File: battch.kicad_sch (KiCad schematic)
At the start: 12 parts, among them IC1 SI3483DDV-T1-BE3, IC2 BQ25302RTER

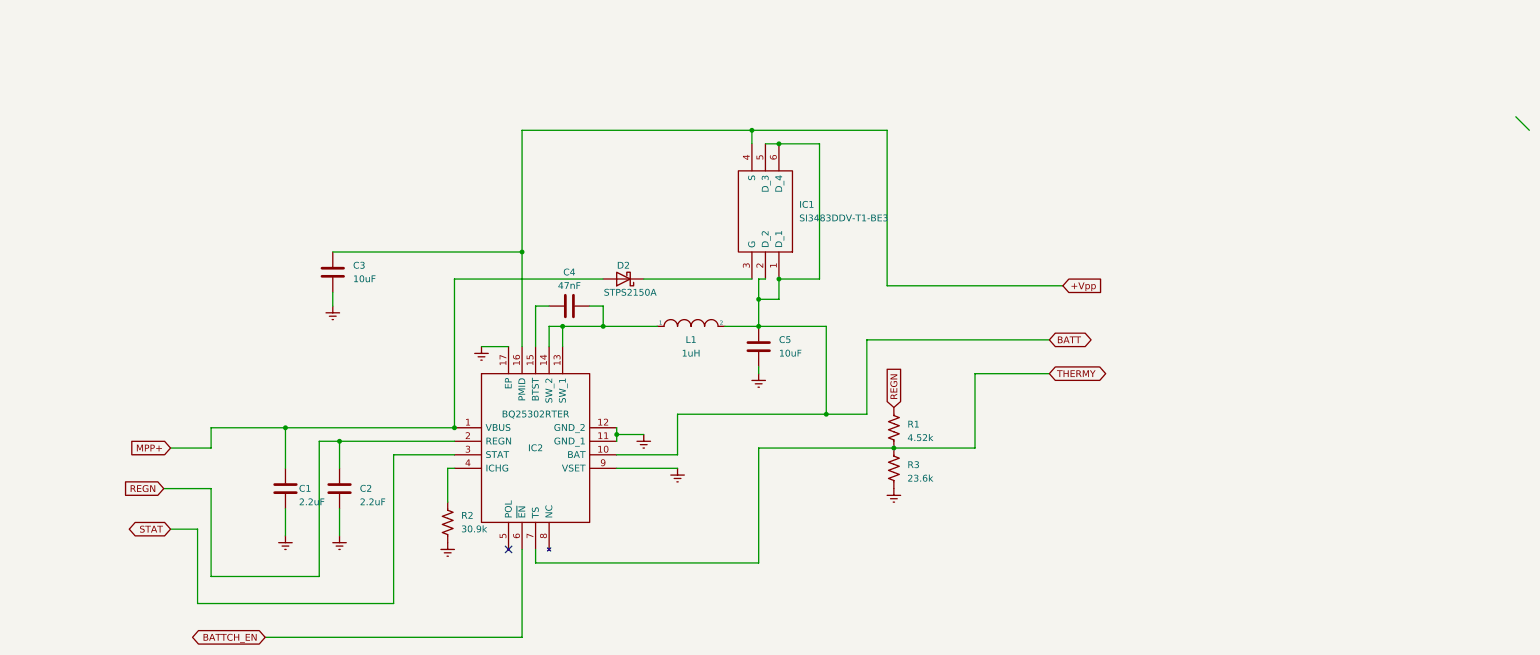
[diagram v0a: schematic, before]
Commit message: Final Schematic
Final Schematic. PC104 pins not assigned.
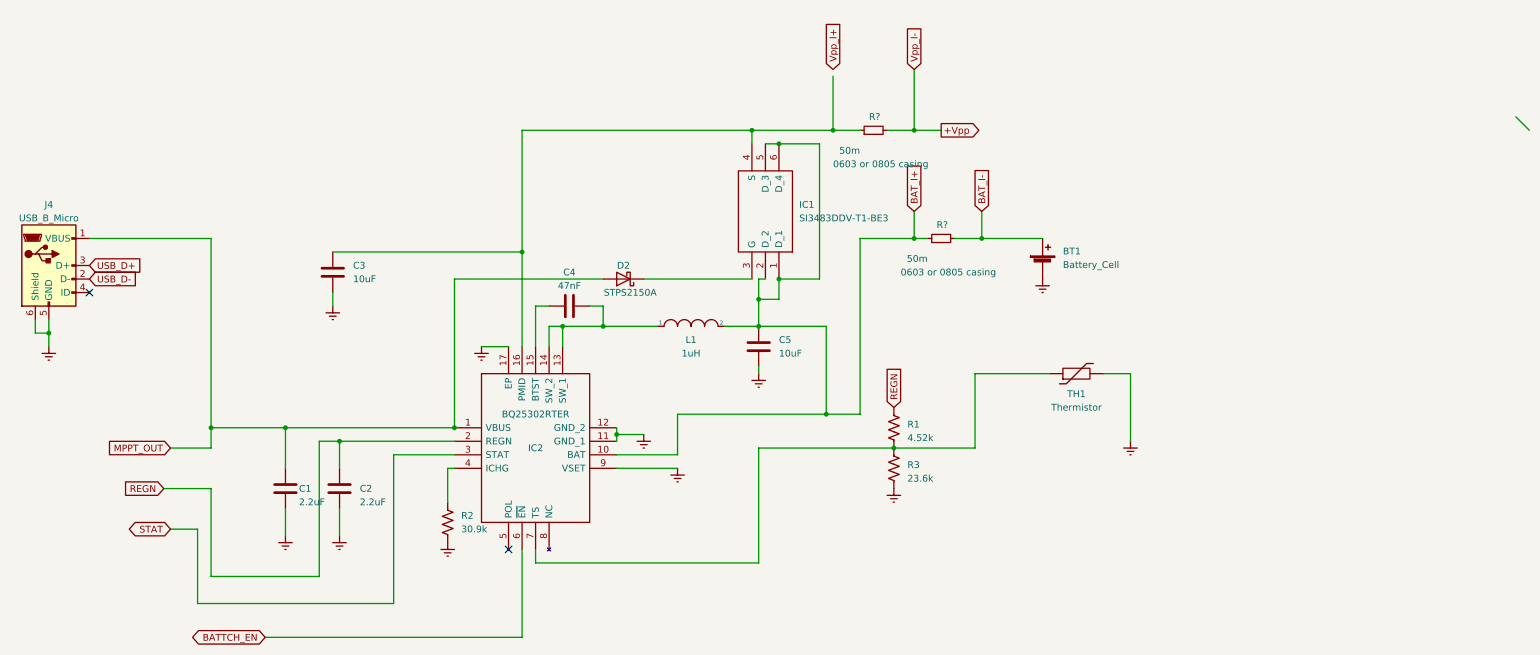
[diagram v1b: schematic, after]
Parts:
- added BT1: Battery_Cell, symbol Device:Battery_Cell
- added J4: USB_B_Micro, symbol Connector:USB_B_Micro
- added R? (x2): 50m, symbol Device:R_Small
- added TH1: Thermistor, symbol Device:Thermistor
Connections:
- net +Vpp: now also R?.2; no longer C3.1, IC1.4 (S), IC2.16 (PMID)
- net Earth: now also BT1.2 (-), J4.5 (GND), J4.6 (Shield), TH1.2
- net BATT renamed BAT_I+
- net BAT_I+: now also R?.1
- net MPP+ renamed MPPT_OUT
- net MPPT_OUT: now also J4.1 (VBUS)
- net THERMY: no longer names the net of IC2.7 (TS), R1.1, R3.2
- net THERMY: now also TH1.1
- new net: C3.1, IC1.4 (S), IC2.16 (PMID), R?.1
- new net BAT_I-: BT1.1 (+), R?.2
- new net USB_D+: J4.3 (D+)
- new net USB_D-: J4.2 (D-)
- no-connect marks 1 -> 2

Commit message: Ready to rearrange
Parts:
- BT1: footprint (none) -> Battery:BatteryHolder_Keystone_1042_1x18650
- J4: footprint (none) -> usbb:USB_Micro-B_Amphenol_10118194_Horizontal
- R? (x2): footprint (none) -> Resistor_SMD:R_0805_2012Metric
- TH1: footprint (none) -> Thermmy:103AT2
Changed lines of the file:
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@@
       (effects (font (size 1.27 1.27)))
     )
-    (property "Footprint" "" (at 238.76 85.09 0)
+    (property "Footprint" "Thermmy:103AT2" (at 238.76 85.09 0)
       (effects (font (size 1.27 1.27)) hide)
     )
@@
       (effects (font (size 1.27 1.27)) (justify left))
     )
-    (property "Footprint" "" (at 213.36 59.69 0)
+    (property "Footprint" "Resistor_SMD:R_0805_2012Metric" (at 213.36 59.69 0)
       (effects (font (size 1.27 1.27)) hide)
     )
@@
       (effects (font (size 1.27 1.27)))
     )
-    (property "Footprint" "" (at 49.53 66.04 0)
+    (property "Footprint" "usbb:USB_Micro-B_Amphenol_10118194_Horizontal" (at 49.53 66.04 0)
       (effects (font (size 1.27 1.27)) hide)
     )
@@
       (effects (font (size 1.27 1.27)) (justify left))
     )
-    (property "Footprint" "" (at 200.66 39.37 0)
+    (property "Footprint" "Resistor_SMD:R_0805_2012Metric" (at 200.66 39.37 0)
       (effects (font (size 1.27 1.27)) hide)
     )
@@
       (effects (font (size 1.27 1.27)) (justify left))
     )
-    (property "Footprint" "" (at 232.41 63.246 90)
-      (effects (font (size 1.27 1.27)) hide)
-    )
+    (property "Footprint" "Battery:BatteryHolder_Keystone_1042_1x18650" (at 232.41 63.246 90)
+      (effects (font (size 1.27 1.27)) hide)
+    )
